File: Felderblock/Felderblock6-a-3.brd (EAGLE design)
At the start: 78.7 x 99.1 mm, 41 parts, among them IC1 MCP23017SP, X1 JP5-FLAT, X2 JP5-FLATFEMALE

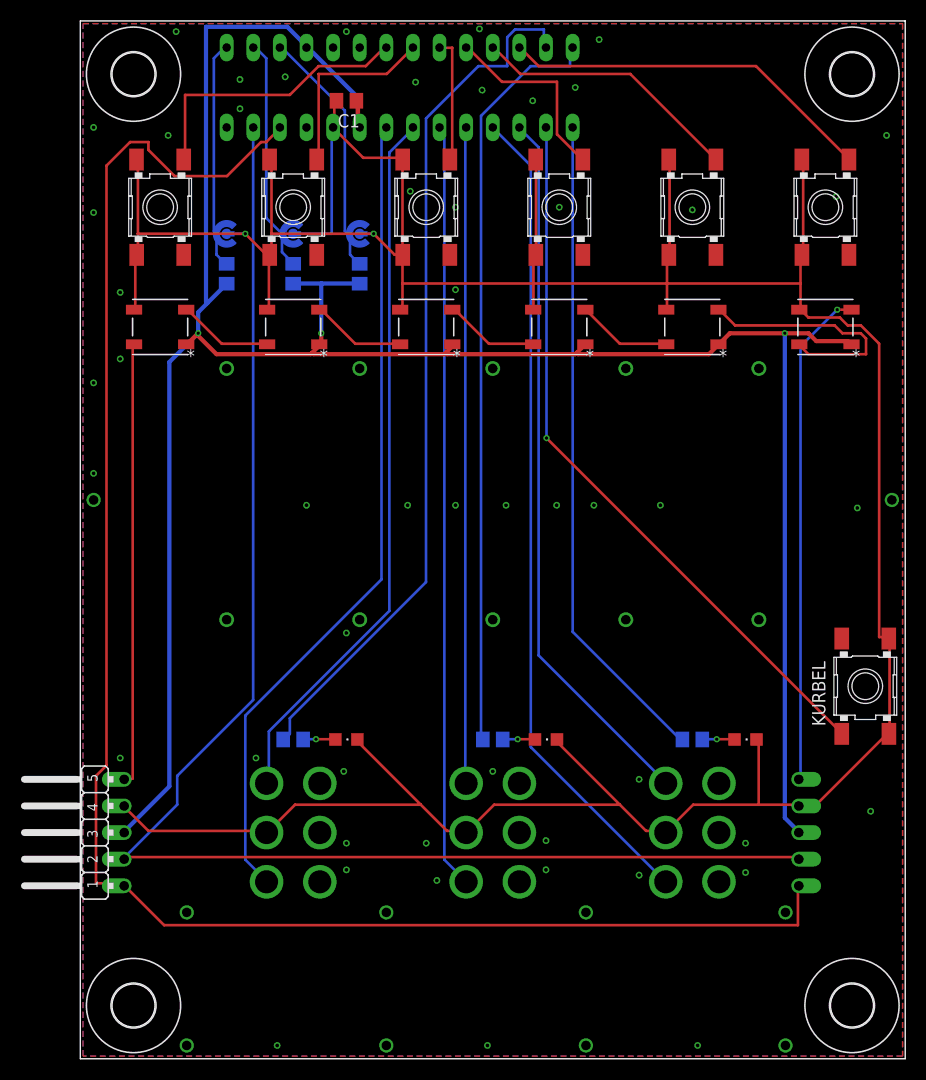
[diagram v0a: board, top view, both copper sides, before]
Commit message: Adds labels for IO port.
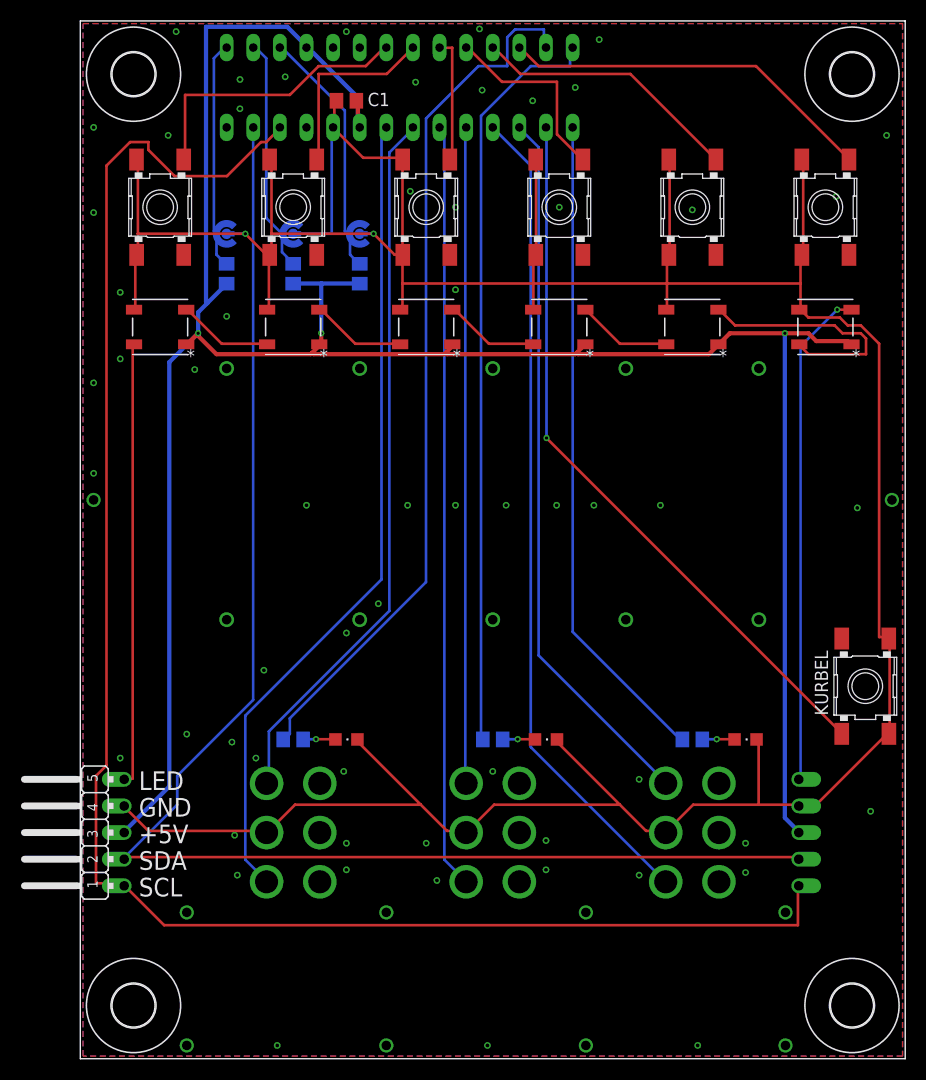
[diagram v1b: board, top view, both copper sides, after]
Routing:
- net GND: vias 54 -> 62
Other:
- board text added: "+5V"
- board text added: "GND"
- board text added: "LED"
- board text added: "SCL"
- board text added: "SDA"
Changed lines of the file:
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@@
 <setting verticaltext="up"/>
 </settings>
-<grid distance="10" unitdist="mil" unit="mm" style="lines" multiple="1" display="yes" altdistance="5" altunitdist="mil" altunit="mil"/>
+<grid distance="10" unitdist="mil" unit="mil" style="lines" multiple="1" display="yes" altdistance="5" altunitdist="mil" altunit="mil"/>
 <layers>
 <layer number="1" name="Top" color="4" fill="1" visible="yes" active="yes"/>
@@
 <wire x1="78.74" y1="99.06" x2="0" y2="99.06" width="0" layer="20"/>
 <wire x1="0" y1="99.06" x2="0" y2="0" width="0" layer="20"/>
+<text x="5.588" y="15.494" size="1.778" layer="25">SCL</text>
+<text x="5.588" y="18.034" size="1.778" layer="25">SDA</text>
+<text x="5.588" y="20.574" size="1.778" layer="25">+5V</text>
+<text x="5.588" y="23.114" size="1.778" layer="25">GND</text>
+<text x="5.588" y="25.654" size="1.778" layer="25">LED</text>
 </plain>
 <attributes>
@@
 </element>
 <element name="KURBEL" library="g-e2e-training" package="TACTSW-6X6" value="W1" x="74.93" y="35.56" smashed="yes" rot="R270">
-<attribute name="NAME" x="71.12" y="31.75" size="1.27" layer="25" rot="R90"/>
+<attribute name="NAME" x="71.374" y="32.766" size="1.27" layer="25" font="vector" rot="R90"/>
 <attribute name="VALUE" x="70.485" y="38.1" size="1.27" layer="27" rot="R270"/>
 </element>
@@
 </element>
 <element name="C1" library="rcl" library_urn="urn:adsk.eagle:library:334" package="C0805" package3d_urn="urn:adsk.eagle:package:23617/2" value="" x="25.4" y="91.44" smashed="yes" rot="R180">
-<attribute name="NAME" x="26.67" y="90.17" size="1.27" layer="25" rot="R180"/>
+<attribute name="NAME" x="27.432" y="90.932" size="1.27" layer="25"/>
 <attribute name="POPULARITY" value="88" x="25.4" y="91.44" size="1.778" layer="27" rot="R180" display="off"/>
 <attribute name="SPICEPREFIX" value="C" x="25.4" y="91.44" size="1.778" layer="27" rot="R180" display="off"/>
@@
 <via x="15.75" y="78.75" extent="1-16" drill="0.3048"/>
 <via x="28" y="78.75" extent="1-16" drill="0.3048"/>
-<polygon width="0.1524" layer="1">
+<polygon width="0.1524" layer="1" isolate="0.254">
 <vertex x="0.254" y="98.806"/>
 <vertex x="78.486" y="98.806"/>
@@
 <vertex x="0.254" y="0.254"/>
 </polygon>
-<polygon width="0.1524" layer="16">
+<polygon width="0.1524" layer="16" isolate="0.254">
 <vertex x="0.254" y="98.806"/>
 <vertex x="78.486" y="98.806"/>
@@
 <via x="35.814" y="81.28" extent="1-16" drill="0.35"/>
 <via x="35.814" y="73.406" extent="1-16" drill="0.35"/>
+<via x="10.16" y="30.988" extent="1-16" drill="0.35"/>
+<via x="10.922" y="65.786" extent="1-16" drill="0.35"/>
+<via x="13.97" y="70.866" extent="1-16" drill="0.35"/>
+<via x="17.526" y="37.084" extent="1-16" drill="0.35"/>
+<via x="28.448" y="43.434" extent="1-16" drill="0.35"/>
+<via x="14.478" y="30.226" extent="1-16" drill="0.35"/>
+<via x="14.732" y="21.336" extent="1-16" drill="0.35"/>
+<via x="14.986" y="17.526" extent="1-16" drill="0.35"/>
 </signal>
 <signal name="+5V" class="1">
